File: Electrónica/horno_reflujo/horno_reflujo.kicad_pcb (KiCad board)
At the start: 2 copper layers, 100 x 80 mm, 46 parts, among them J1 LevelShifter, J10 ssr1, J11 ssr2, J12 encoder, J13 Max6675_modulo2, J14 Max6675_modulo3, J15 Max6675_modulo4, J2 LevelShifter, J3 Display Oled I2C, J4 Max6675_modulo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

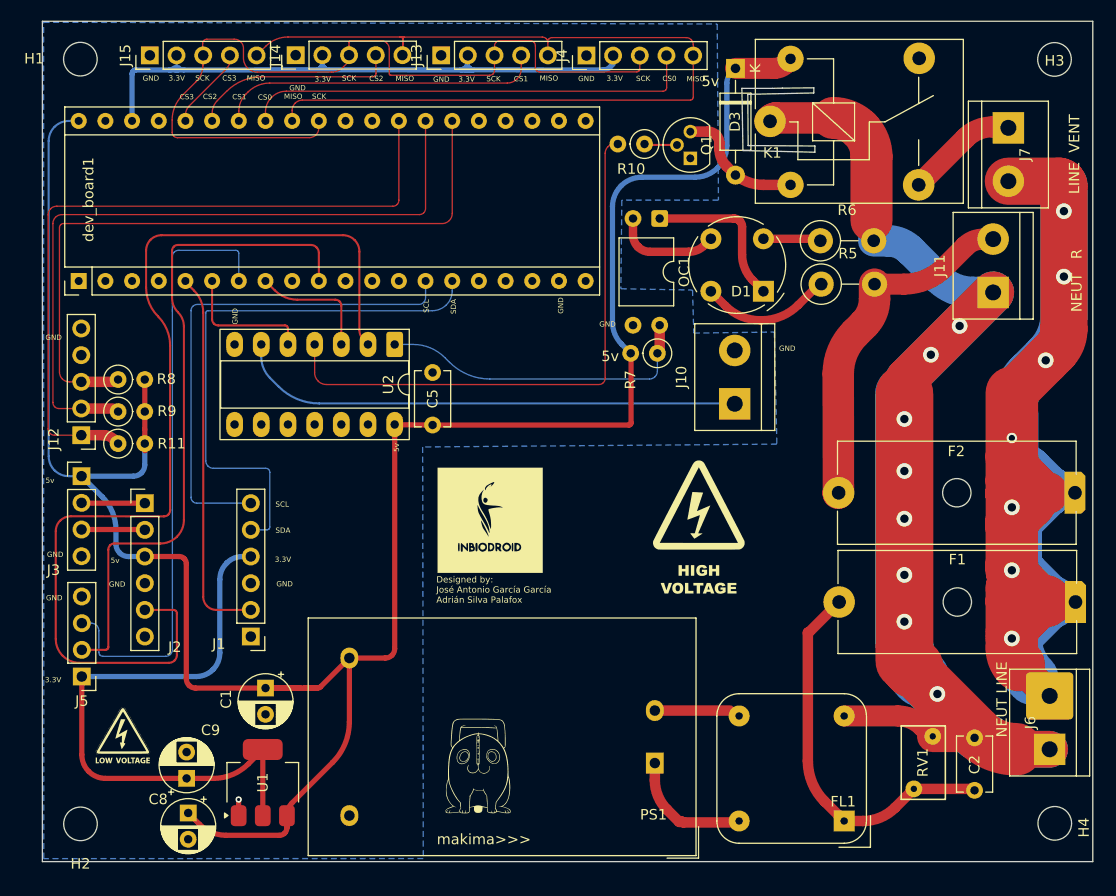
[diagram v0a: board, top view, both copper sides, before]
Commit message: mcu pin update
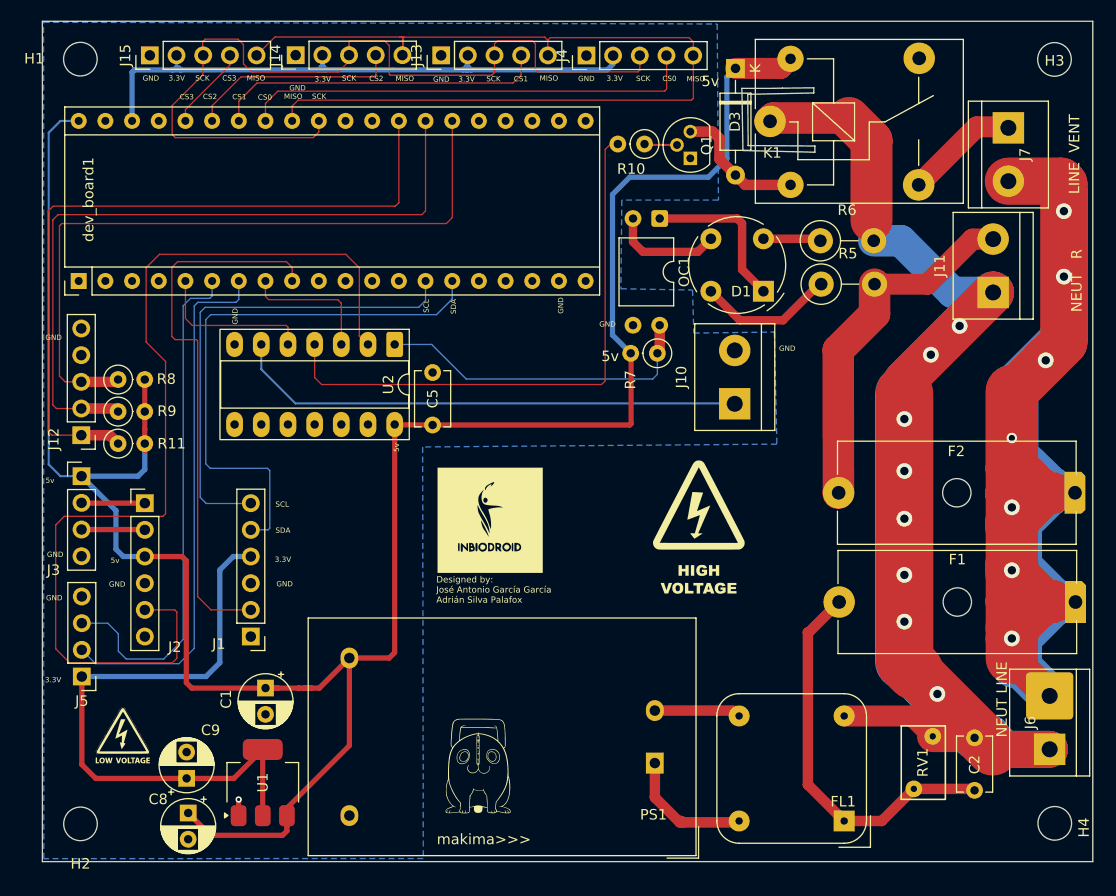
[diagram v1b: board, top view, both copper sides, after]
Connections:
- dev_board1 pad 10: /Rx_mcu_esp01 -> unconnected-(dev_board1-A15-Pad10)
- dev_board1 pad 5: /zc -> /fire
- dev_board1 pad 6: /fire -> /Tx_mcu_esp01
- dev_board1 pad 7: /Tx_mcu_esp01 -> /Rx_mcu_esp01
- dev_board1 pad 9: unconnected-(dev_board1-A12-Pad9) -> /zc
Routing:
- net /zc: track 36.6 -> 52.7 mm
- net /Rx_mcu_esp01: track 64.0 -> 50.7 mm
- net /Tx_mcu_esp01: track 59.0 -> 49.6 mm
- net zero: track 99.1 -> 95.7 mm
- net /fire: track 12.9 -> 15.9 mm
- net +3.3Vmc: track 60.7 -> 58.6 mm
- net I2C1_SCL: track 48.6 -> 47.1 mm
- net /fan: track 11.8 -> 12.9 mm
- net SPI1_SCK: track 82.0 -> 83.1 mm
- net NEUT: track 172.0 -> 171.2 mm
- net Net-(J11-Pin_2): track 33.6 -> 34.4 mm
- net Net-(D3-A): track 12.7 -> 13.5 mm
- net Net-(OC1-Pad4): track 30.8 -> 31.3 mm
- net Net-(C2-Pad1): track 36.8 -> 37.3 mm

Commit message: Update pcb
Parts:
- moved G*** 2.62 mm to (78.7, 95.8)
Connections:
- J1 pad 3: GND -> +3.3V
- J1 pad 4: +3.3V -> GND
- J2 pad 3: +5V -> GND
- J2 pad 4: GND -> +5V
- J3 pad 1: +5V -> GND
- J3 pad 2: Net-(J2-Pin_1) -> +5V
- J3 pad 3: Net-(J2-Pin_2) -> Net-(J2-Pin_1)
- J3 pad 4: GND -> Net-(J2-Pin_2)
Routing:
- net NEUT: track 171.2 -> 161.2 mm
- net LINE: track 177.5 -> 170.9 mm
- net zero: track 95.7 -> 93.0 mm
- net +5V: track 227.4 -> 225.0 mm
- net +3.3Vmc: track 58.6 -> 60.7 mm
- net Net-(J10-Pin_1): track 48.8 -> 47.3 mm
- net +3.3V: track 61.1 -> 59.8 mm
- net /Tx_mcu_esp01: track 49.6 -> 48.3 mm
- net SPI1_SCK: track 83.1 -> 82.1 mm
- net Net-(J2-Pin_2): track 6.04 -> 6.99 mm
- net Net-(J2-Pin_1): track 6.04 -> 6.93 mm
- net /Rx_mcu_esp01: track 50.7 -> 49.9 mm
- net Net-(D3-A): track 13.5 -> 12.7 mm
- net GND: track 2.46 -> 1.84 mm
- net /zc: track 52.7 -> 52.2 mm
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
